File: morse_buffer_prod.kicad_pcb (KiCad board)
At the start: 2 copper layers, 99.7 x 90.8 mm, 107 parts, among them J1 Columns, J2 EXT_SW, J3 Rows, J4 TRIG_OUT, J5 Barrel_Jack_Switch, K1 G5V-1, Q1 MMBT2222A, Q2 MMBT2222A, Q3 NCE30P12S, Q4 MMBT2222A, SW1 M_RST, SW2 BTN, SW3 OUTPUT_SEL, U1 NE555D, U10 74HC138, U11 74HC138, U12 IDT7201LA50TP, U13 MORSE_EEPROM, U14 LENGTH_EEPROM, U15 74HC151, U16 74HC688, U17 74HC221, U18 74HC74, U19 74HC161, U2 NE555D, U20 74HC161, U21 PC817, U3 74HC32, U4 74HC32, U5 74HC14, U6 74HC10, U7 74HC74, U8 74HC74, U9 74HC161

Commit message: PCB routing
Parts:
- removed C21: 10nF, Capacitor_SMD:C_0603_1608Metric
- removed C22: 10uF, Capacitor_THT:CP_Radial_D5.0mm_P2.00mm
- removed D1: TX/WAIT, LED_SMD:LED_0603_1608Metric
- removed J3: Rows, Connector_PinHeader_2.54mm:PinHeader_1x04_P2.54mm_Vertical
- removed Q4: MMBT2222A, Package_TO_SOT_SMD:SOT-23
- removed the R11 at (113.0, 141.6)
- removed the R16 at (80.0, 95.9)
- removed R21, R26, R27: 4K7, Resistor_SMD:R_0603_1608Metric
- removed the R4 at (75.2, 117.1)
- removed the R6 at (105.4, 141.6)
- removed the R7 at (123.2, 141.6)
- removed the R8 at (108.0, 141.6)
- removed the R9 at (110.5, 141.6)
- added R2: 4K7, Resistor_SMD:R_0603_1608Metric, F.Cu at (71.8, 142.1)
- added R3: 1K, Resistor_SMD:R_0603_1608Metric, F.Cu at (67.9, 138.4)
- J1: value Columns -> Keyboard; footprint Connector_PinHeader_2.54mm:PinHeader_1x13_P2.54mm_Vertical -> GiraffeTech-Connector:Connector_Mini-DIN_Female_6Pin_2rows
- R1: value 470R -> 4K7
- U1: value NE555D -> 74HC74; footprint Package_SO:SOIC-8_3.9x4.9mm_P1.27mm -> Package_SO:SOIC-14_3.9x8.7mm_P1.27mm
- U10: value 74HC138 -> 74HC280; footprint Package_SO:SOIC-16_3.9x9.9mm_P1.27mm -> Package_SO:SOIC-14_3.9x8.7mm_P1.27mm
- U11: value 74HC138 -> 74HC11; footprint Package_SO:SOIC-16_3.9x9.9mm_P1.27mm -> Package_SO:SOIC-14_3.9x8.7mm_P1.27mm
- U3: value 74HC32 -> 74HC14
- U7, U8: value 74HC74 -> 74HC164
- moved U1 47.6 mm to (120.0, 132.7)
- moved U3 45.7 mm to (90.8, 121.9)
- moved Q2 45.0 mm to (67.9, 142.4), turned to 0 degrees
- moved U9 44.5 mm to (134.6, 132.7)
- moved U7 30.5 mm to (75.6, 132.7)
- moved U8 29.2 mm to (90.8, 132.7)
- moved R1 22.0 mm to (71.8, 139.1)
- moved J1 15.1 mm to (83.8, 142.1), turned to 0 degrees
- moved U11 14.6 mm to (106.0, 132.7)
- moved U10 10.8 mm to (75.6, 121.9)
- moved R4 9.86 mm to (87.0, 75.8), turned to 180 degrees
- moved H1 7.11 mm to (68.2, 147.8)
- moved D10 5.10 mm to (123.2, 145.4)
- moved R5 5.10 mm to (123.2, 141.6)
- moved RV1 4.83 mm to (73.5, 96.5)
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- renumbered C8 to C1, C1 to C10, C7 to C11, C9 to C3, C10 to C7, C11 to C8, C3 to C9, R2 to R10, R15 to R11, R13 to R12, R22 to R13, R23 to R15, R17 to R16, R18 to R17, R19 to R18, R20 to R19, R24 to R4, R25 to R5, R3 to R6, R5 to R7, R12 to R8, R10 to R9
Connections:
- J1 pad 1: Net-(J1-Pad1) -> KBDAT
- J1 pad 3: Net-(J1-Pad3) -> GNDREF
- J1 pad 4: Net-(J1-Pad4) -> +5V
- J1 pad 5: Net-(J1-Pad5) -> KBCLK
- J1 pad 7: Net-(J1-Pad7) -> (no net)
- Q2 pad 3: TX_COMPLETE -> KBCLK
- R1 pad 2: Net-(R1-Pad2) -> KBCLK
- U1 pad 1: GNDREF -> +5V
- U1 pad 2: Net-(C22-Pad1) -> GNDREF
- U1 pad 3: /58Hz_Square -> KBD_END
- U1 pad 4: ~FULL -> ~KB_BREAK
- U1 pad 5: Net-(C21-Pad1) -> Net-(U1-Pad12)
- U1 pad 6: Net-(C22-Pad1) -> Net-(U1-Pad6)
- U1 pad 7: Net-(R1-Pad2) -> GNDREF
- U1 pad 8: +5V -> Net-(U1-Pad8)
- U10 pad 1: COL_0 -> KBD2
- U10 pad 10: Net-(J1-Pad6) -> KBD6
- U10 pad 11: Net-(J1-Pad5) -> KBD5
- U10 pad 12: Net-(J1-Pad4) -> KBD4
- U10 pad 13: Net-(J1-Pad3) -> KBD3
- U10 pad 14: Net-(J1-Pad2) -> +5V
- U10 pad 2: COL_1 -> KBDP
- U10 pad 3: COL_2 -> Net-(U10-Pad3)
- U10 pad 4: GNDREF -> KBD7
- U10 pad 5: COL_3 -> Net-(U10-Pad5)
- U10 pad 6: +5V -> KBD_VALID
- U10 pad 7: Net-(J1-Pad8) -> GNDREF
- U10 pad 8: GNDREF -> KBD0
- U10 pad 9: Net-(J1-Pad7) -> KBD1
- U11 pad 1: COL_0 -> KBD_VALID
- U11 pad 11: Net-(J1-Pad13) -> Net-(U11-Pad11)
- U11 pad 12: Net-(J1-Pad12) -> KEYBOARD_PRESS
- U11 pad 13: Net-(J1-Pad11) -> KBD_END
- U11 pad 14: Net-(J1-Pad10) -> +5V
- U11 pad 2: COL_1 -> ~KB_INHIBIT
- U11 pad 3: COL_2 -> KBD5
- U11 pad 4: GNDREF -> KBD6
- U11 pad 5: GNDREF -> KBD7
- U11 pad 6: COL_3 -> Net-(U11-Pad6)
- U11 pad 7: Net-(U11-Pad7) -> GNDREF
- U11 pad 8: GNDREF -> KBD_END
- U12 pad 24: ROW_3 -> KBD7
- U12 pad 25: ROW_2 -> KBD6
- U12 pad 26: ROW_1 -> KBD5
- U12 pad 27: ROW_0 -> KBD4
- U12 pad 3: COL_3 -> KBD3
- U12 pad 4: COL_2 -> KBD2
- U12 pad 5: COL_1 -> KBD1
- U12 pad 6: COL_0 -> KBD0
- U16 pad 19: Net-(R21-Pad2) -> Net-(U16-Pad19)
- U19 pad 2: Net-(Q4-Pad3) -> Net-(U19-Pad2)
- U2 pad 3: Net-(R27-Pad2) -> Net-(U2-Pad3)
- U20 pad 2: Net-(Q4-Pad3) -> Net-(U19-Pad2)
- U3 pad 1: ROW_2 -> GNDREF
- U3 pad 10: Net-(U3-Pad10) -> TX_COMPLETE
- U3 pad 11: Net-(U3-Pad11) -> Net-(U16-Pad19)
- U3 pad 12: /58Hz_Square -> Net-(U19-Pad2)
- U3 pad 13: KEYBOARD_PRESS -> Net-(U2-Pad3)
- U3 pad 2: ROW_3 -> Net-(U3-Pad2)
- U3 pad 3: Net-(U3-Pad10) -> KBCLK
- U3 pad 4: ROW_0 -> ~KBCLK
- U3 pad 5: ROW_1 -> GNDREF
- U3 pad 8: KEYBOARD_PRESS -> Net-(R3-Pad2)
- U3 pad 9: Net-(U3-Pad6) -> ~FULL
- U4 pad 1: RD_RESET -> Net-(U1-Pad6)
- U4 pad 2: Net-(U4-Pad2) -> Net-(U1-Pad8)
- U4 pad 3: Net-(U4-Pad3) -> ~KB_INHIBIT
- U5 pad 1: Net-(U3-Pad11) -> TX_RESET
- U5 pad 2: Net-(U5-Pad2) -> ~TX_RESET
- U5 pad 3: Net-(U4-Pad3) -> GNDREF
- U5 pad 5: ~FULL -> RD_RESET
- U5 pad 6: Net-(U4-Pad2) -> Net-(U5-Pad6)
- U6 pad 1: TX_RESET -> Net-(U11-Pad6)
- U6 pad 12: ~TX_RESET -> ~KB_BREAK
- U6 pad 13: TX_RESET -> KBD4
- U6 pad 2: TX_RESET -> Net-(U11-Pad6)
- U7 pad 1: +5V -> KBDAT
- U7 pad 10: Net-(U5-Pad4) -> KBD5
- U7 pad 11: Net-(U3-Pad11) -> KBD4
- U7 pad 12: Net-(J3-Pad2) -> KBD3
- U7 pad 13: +5V -> KBD2
- U7 pad 2: Net-(J3-Pad1) -> KBDAT
- U7 pad 3: Net-(U3-Pad11) -> Net-(U7-Pad3)
- U7 pad 4: Net-(U5-Pad4) -> KBDP
- U7 pad 5: Net-(U7-Pad5) -> KBD7
- U7 pad 6: ROW_0 -> KBD6
- U7 pad 8: ROW_1 -> ~KBCLK
- U7 pad 9: Net-(U7-Pad9) -> +5V
- U8 pad 1: +5V -> KBD2
- U8 pad 10: Net-(U5-Pad4) -> Net-(U8-Pad10)
- U8 pad 11: Net-(U3-Pad11) -> Net-(U8-Pad11)
- U8 pad 13: +5V -> Net-(U8-Pad13)
- U8 pad 2: Net-(J3-Pad3) -> KBD2
- U8 pad 3: Net-(U3-Pad11) -> KBD1
- U8 pad 4: Net-(U5-Pad4) -> KBD0
- U8 pad 6: ROW_2 -> Net-(U8-Pad6)
- U8 pad 8: ROW_3 -> ~KBCLK
- U8 pad 9: Net-(U8-Pad9) -> +5V
- U9 pad 1: +5V -> Net-(U5-Pad6)
- U9 pad 11: COL_3 -> Net-(U11-Pad11)
- U9 pad 12: COL_2 -> Net-(U9-Pad12)
- U9 pad 13: COL_1 -> Net-(U11-Pad10)
- U9 pad 14: COL_0 -> Net-(U11-Pad9)
- U9 pad 2: Net-(U5-Pad2) -> ~KBCLK
- U9 pad 7: +5V -> Net-(U5-Pad6)
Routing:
- net KBD4: track 0.00 -> 150.3 mm, vias 0 -> 3
- net KBD5: track 0.00 -> 95.3 mm, vias 0 -> 2
- net KBD6: track 0.00 -> 93.3 mm, vias 0 -> 2
- net KBD7: track 0.00 -> 93.1 mm, vias 0 -> 2
- net ROW_0: track 86.5 -> 0.00 mm, vias 2 -> 0
- net ROW_1: track 80.9 -> 0.00 mm, vias 2 -> 0
- net ROW_2: track 73.8 -> 0.00 mm, vias 2 -> 0
- net KBD2: track 0.00 -> 72.8 mm, vias 0 -> 4
- net ROW_3: track 70.8 -> 0.00 mm, vias 2 -> 0
- net COL_0: track 66.7 -> 0.00 mm, vias 5 -> 0
- net ~KBCLK: track 0.00 -> 66.2 mm, vias 0 -> 4
- net /58Hz_Square: track 64.4 -> 0.00 mm, vias 2 -> 0
- net KBD0: track 0.00 -> 62.9 mm, vias 0 -> 5
- net KBD1: track 0.00 -> 62.1 mm, vias 0 -> 4
- net COL_1: track 62.1 -> 0.00 mm, vias 4 -> 0
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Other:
- board text added: "74HC11"
- board text added: "74HC164"
- board text added: "74HC280"
- board text added: "Morse Keyboard PR1"
- board text added: "PS/2"
- board text removed: "12"
- board text removed: "3"
- board text removed: "74HC138"
- board text removed: "KEYBOARD COLUMNS"
- board text removed: "Morse Keyboard Rev. 1"
- board text removed: "ROWS"
- board text removed: "WAIT"

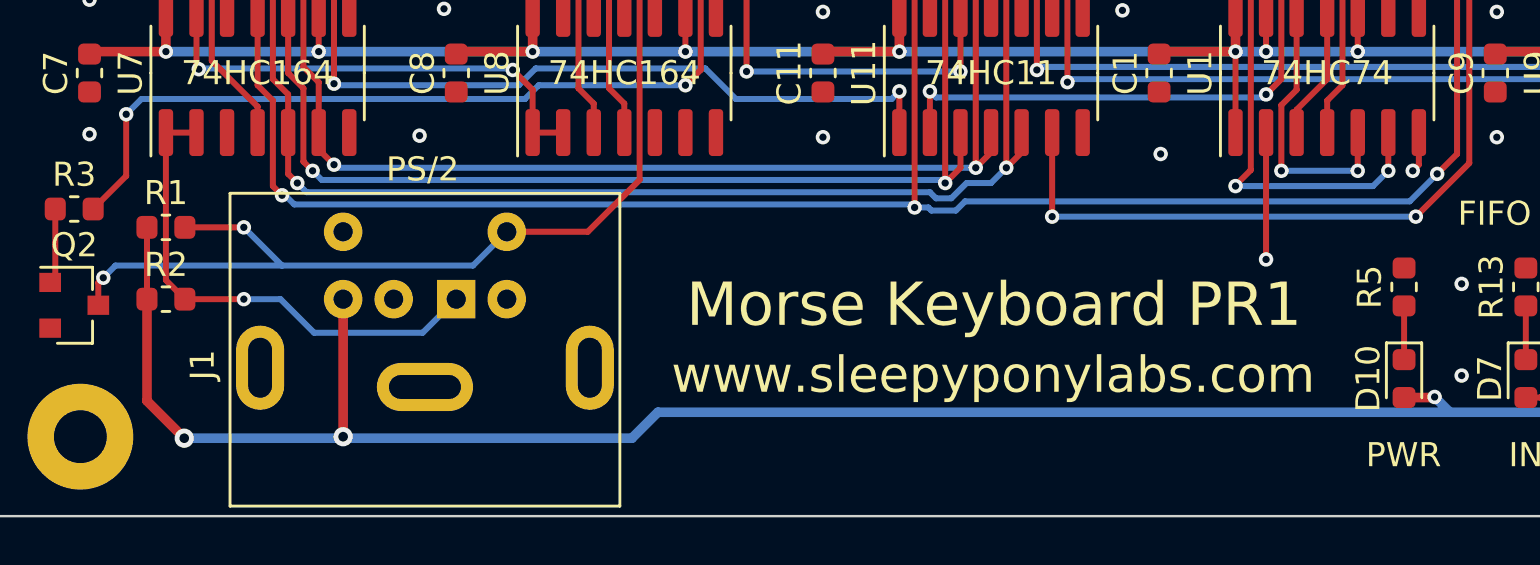
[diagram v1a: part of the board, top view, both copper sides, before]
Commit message: Add fuse for ps/2 device
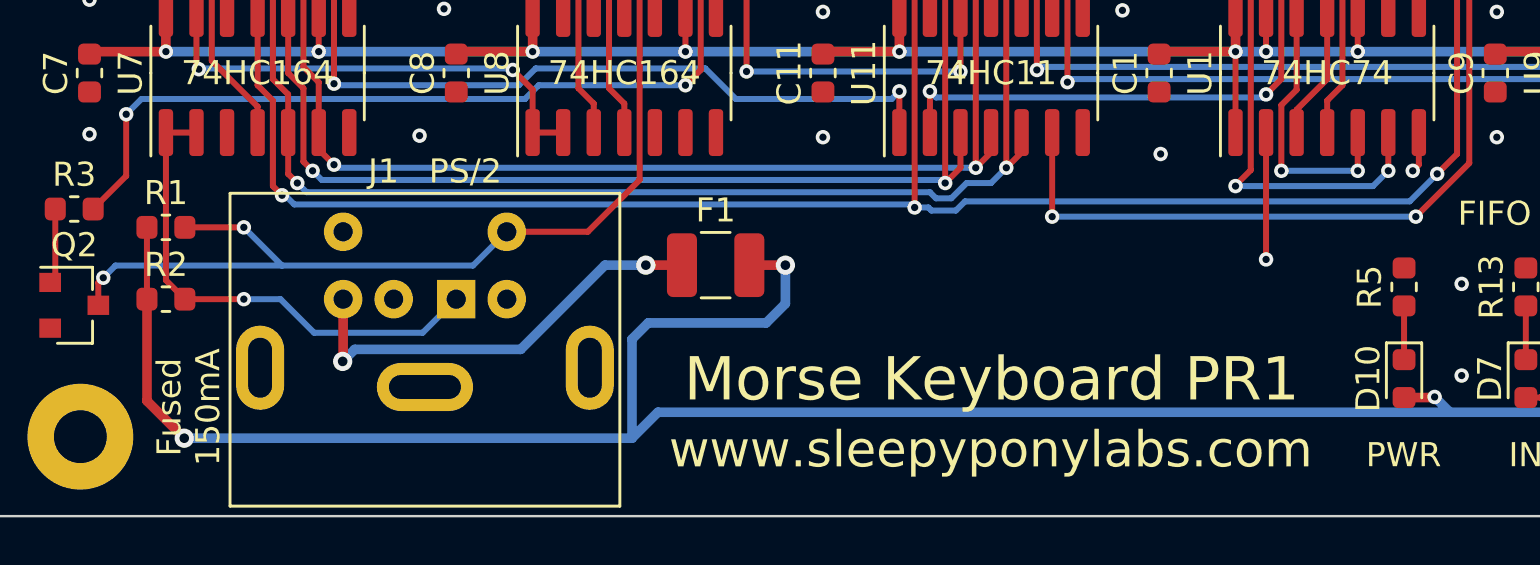
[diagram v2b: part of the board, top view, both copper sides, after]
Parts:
- added F1: 150mA, Fuse:Fuse_1210_3225Metric, F.Cu at (94.6, 140.7)
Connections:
- J1 pad 4: +5V -> Net-(F1-Pad1)
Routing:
- net Net-(F1-Pad1): track 0.00 -> 18.6 mm, vias 0 -> 2
- net +5V: track 770.9 -> 779.0 mm
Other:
- board text added: "Fused 150mA"
